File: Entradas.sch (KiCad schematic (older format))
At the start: 20 parts, among them J3 TB_1X3, U1 PS2805-1, U2 PS2805-1, U3 CNY70

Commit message: Se agrego documentacion del proyecto, se agregaron vistas 3d faltantes y se repararon las extensiones de las que no funcionaban
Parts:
- D5, D6: Digikey# (none) -> 160-1446-1-ND
- ENC1: Digikey# (none) -> 987-1188-ND
- J3: Digikey# (none) -> ED2610-ND
- R10, R16, R5, R8, R9: footprint Resistors_SMD:R_1206_HandSoldering -> Resistors_SMD:R_0805_HandSoldering; Digikey# (none) -> RMCF0805JT4K70TR-ND
- R11, R13: footprint Resistors_SMD:R_1206_HandSoldering -> Resistors_SMD:R_0805_HandSoldering; Digikey# (none) -> RMCF0805JT2K20TR-ND
- R12, R14: footprint Resistors_SMD:R_1206_HandSoldering -> Resistors_SMD:R_0805_HandSoldering; Digikey# (none) -> RMCF0805JT100KTR-ND
- R15: footprint Resistors_SMD:R_1206_HandSoldering -> Resistors_SMD:R_0805_HandSoldering; Digikey# (none) -> RMCF0805JT220RTR-ND
- R17: Digikey# (none) -> PTD901-2015K-B502-ND
- R6, R7: footprint Resistors_SMD:R_1206_HandSoldering -> Resistors_SMD:R_0805_HandSoldering; Digikey# (none) -> RMCF0805JT3K30TR-ND
- U1, U2: Digikey# (none) -> PS2805-1ATR-ND
- U3: Digikey# (none) -> 751-1025-ND
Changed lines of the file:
@@
 F 2 "Potentiometers:Potentiometer_Alps-RK16-single_largePads" H 8100 4650 50  0001 C CNN
 F 3 "" H 8100 4650 50  0000 C CNN
+F 4 "PTD901-2015K-B502-ND" H 8100 4650 60  0001 C CNN "Digikey#"
 	1    8100 4650
 	-1   0    0    1
@@
 F 0 "R9" V 2880 4550 50  0000 C CNN
 F 1 "4K7" V 2800 4550 50  0000 C CNN
-F 2 "Resistors_SMD:R_1206_HandSoldering" V 2730 4550 50  0001 C CNN
+F 2 "Resistors_SMD:R_0805_HandSoldering" V 2730 4550 50  0001 C CNN
 F 3 "" H 2800 4550 50  0000 C CNN
+F 4 "RMCF0805JT4K70TR-ND" H 2800 4550 60  0001 C CNN "Digikey#"
 	1    2800 4550
 	-1   0    0    -1
@@
 F 0 "R5" V 2580 4550 50  0000 C CNN
 F 1 "4K7" V 2500 4550 50  0000 C CNN
-F 2 "Resistors_SMD:R_1206_HandSoldering" V 2430 4550 50  0001 C CNN
+F 2 "Resistors_SMD:R_0805_HandSoldering" V 2430 4550 50  0001 C CNN
 F 3 "" H 2500 4550 50  0000 C CNN
+F 4 "RMCF0805JT4K70TR-ND" H 2500 4550 60  0001 C CNN "Digikey#"
 	1    2500 4550
 	-1   0    0    -1
@@
 F 0 "R8" V 2930 2250 50  0000 C CNN
 F 1 "4K7" V 2850 2250 50  0000 C CNN
-F 2 "Resistors_SMD:R_1206_HandSoldering" V 2780 2250 50  0001 C CNN
+F 2 "Resistors_SMD:R_0805_HandSoldering" V 2780 2250 50  0001 C CNN
 F 3 "" H 2850 2250 50  0000 C CNN
+F 4 "RMCF0805JT4K70TR-ND" H 2850 2250 60  0001 C CNN "Digikey#"
 	1    2850 2250
 	1    0    0    -1
@@
 F 0 "R6" V 2680 2050 50  0000 C CNN
 F 1 "3K3" V 2600 2050 50  0000 C CNN
-F 2 "Resistors_SMD:R_1206_HandSoldering" V 2530 2050 50  0001 C CNN
+F 2 "Resistors_SMD:R_0805_HandSoldering" V 2530 2050 50  0001 C CNN
 F 3 "" H 2600 2050 50  0000 C CNN
+F 4 "RMCF0805JT3K30TR-ND" H 2600 2050 60  0001 C CNN "Digikey#"
 	1    2600 2050
 	0    1    1    0
@@
 F 0 "R11" V 4780 1900 50  0000 C CNN
 F 1 "2K2" V 4700 1900 50  0000 C CNN
-F 2 "Resistors_SMD:R_1206_HandSoldering" V 4630 1900 50  0001 C CNN
+F 2 "Resistors_SMD:R_0805_HandSoldering" V 4630 1900 50  0001 C CNN
 F 3 "" H 4700 1900 50  0000 C CNN
+F 4 "RMCF0805JT2K20TR-ND" H 4700 1900 60  0001 C CNN "Digikey#"
 	1    4700 1900
 	0    1    1    0
@@
 F 0 "R12" V 4780 2150 50  0000 C CNN
 F 1 "100K" V 4700 2150 50  0000 C CNN
-F 2 "Resistors_SMD:R_1206_HandSoldering" V 4630 2150 50  0001 C CNN
+F 2 "Resistors_SMD:R_0805_HandSoldering" V 4630 2150 50  0001 C CNN
 F 3 "" H 4700 2150 50  0000 C CNN
+F 4 "RMCF0805JT100KTR-ND" H 4700 2150 60  0001 C CNN "Digikey#"
 	1    4700 2150
 	0    1    1    0
@@
 F 2 "LEDs:LED_0603" H 4200 1900 50  0001 C CNN
 F 3 "" H 4200 1900 50  0000 C CNN
+F 4 "160-1446-1-ND" H 4200 1900 60  0001 C CNN "Digikey#"
 	1    4200 1900
 	1    0    0    -1
@@
 F 2 "Opto-Devices:Optocoupler_SMD_HandSoldering_KPC357_LTV35x_PC357_SingleChannel" H 3236 2076 29  0001 C CNN
 F 3 "" H 3400 2250 60  0000 C CNN
+F 4 "PS2805-1ATR-ND" H 3400 2250 60  0001 C CNN "Digikey#"
 	1    3400 2250
 	1    0    0    -1
@@
 F 2 "footprint:CNY70" H 7400 1950 50  0001 L CIN
 F 3 "" H 7600 2150 50  0000 L CNN
+F 4 "751-1025-ND" H 7600 2150 60  0001 C CNN "Digikey#"
 	1    7600 2150
 	1    0    0    -1
@@
 F 0 "R15" V 7330 2550 50  0000 C CNN
 F 1 "220" V 7250 2550 50  0000 C CNN
-F 2 "Resistors_SMD:R_1206_HandSoldering" V 7180 2550 50  0001 C CNN
+F 2 "Resistors_SMD:R_0805_HandSoldering" V 7180 2550 50  0001 C CNN
 F 3 "" H 7250 2550 50  0000 C CNN
+F 4 "RMCF0805JT220RTR-ND" H 7250 2550 60  0001 C CNN "Digikey#"
 	1    7250 2550
 	1    0    0    -1
@@
 F 0 "R16" V 8030 2550 50  0000 C CNN
 F 1 "4K7" V 7950 2550 50  0000 C CNN
-F 2 "Resistors_SMD:R_1206_HandSoldering" V 7880 2550 50  0001 C CNN
+F 2 "Resistors_SMD:R_0805_HandSoldering" V 7880 2550 50  0001 C CNN
 F 3 "" H 7950 2550 50  0000 C CNN
+F 4 "RMCF0805JT4K70TR-ND" H 7950 2550 60  0001 C CNN "Digikey#"
 	1    7950 2550
 	1    0    0    -1
@@
 F 2 "footprint:Encoder_rotativo" H 3700 5050 50  0001 C CNN
 F 3 "" H 3700 5050 50  0000 C CNN
+F 4 "987-1188-ND" H 3700 5050 60  0001 C CNN "Digikey#"
 	1    3700 5050
 	-1   0    0    -1
@@
 F 0 "R10" V 2930 3000 50  0000 C CNN
 F 1 "4K7" V 2850 3000 50  0000 C CNN
-F 2 "Resistors_SMD:R_1206_HandSoldering" V 2780 3000 50  0001 C CNN
+F 2 "Resistors_SMD:R_0805_HandSoldering" V 2780 3000 50  0001 C CNN
 F 3 "" H 2850 3000 50  0000 C CNN
+F 4 "RMCF0805JT4K70TR-ND" H 2850 3000 60  0001 C CNN "Digikey#"
 	1    2850 3000
 	1    0    0    -1
@@
 F 0 "R7" V 2680 2800 50  0000 C CNN
 F 1 "3K3" V 2600 2800 50  0000 C CNN
-F 2 "Resistors_SMD:R_1206_HandSoldering" V 2530 2800 50  0001 C CNN
+F 2 "Resistors_SMD:R_0805_HandSoldering" V 2530 2800 50  0001 C CNN
 F 3 "" H 2600 2800 50  0000 C CNN
+F 4 "RMCF0805JT3K30TR-ND" H 2600 2800 60  0001 C CNN "Digikey#"
 	1    2600 2800
 	0    1    1    0
@@
 F 0 "R13" V 4780 2650 50  0000 C CNN
 F 1 "2K2" V 4700 2650 50  0000 C CNN
-F 2 "Resistors_SMD:R_1206_HandSoldering" V 4630 2650 50  0001 C CNN
+F 2 "Resistors_SMD:R_0805_HandSoldering" V 4630 2650 50  0001 C CNN
 F 3 "" H 4700 2650 50  0000 C CNN
+F 4 "RMCF0805JT2K20TR-ND" H 4700 2650 60  0001 C CNN "Digikey#"
 	1    4700 2650
 	0    1    1    0
@@
 F 0 "R14" V 4780 2900 50  0000 C CNN
 F 1 "100K" V 4700 2900 50  0000 C CNN
-F 2 "Resistors_SMD:R_1206_HandSoldering" V 4630 2900 50  0001 C CNN
+F 2 "Resistors_SMD:R_0805_HandSoldering" V 4630 2900 50  0001 C CNN
 F 3 "" H 4700 2900 50  0000 C CNN
+F 4 "RMCF0805JT100KTR-ND" H 4700 2900 60  0001 C CNN "Digikey#"
 	1    4700 2900
 	0    1    1    0
@@
 F 2 "LEDs:LED_0603" H 4200 2650 50  0001 C CNN
 F 3 "" H 4200 2650 50  0000 C CNN
+F 4 "160-1446-1-ND" H 4200 2650 60  0001 C CNN "Digikey#"
 	1    4200 2650
 	1    0    0    -1
@@
 F 2 "Opto-Devices:Optocoupler_SMD_HandSoldering_KPC357_LTV35x_PC357_SingleChannel" H 3236 2826 29  0001 C CNN
 F 3 "" H 3400 3000 60  0000 C CNN
+F 4 "PS2805-1ATR-ND" H 3400 3000 60  0001 C CNN "Digikey#"
 	1    3400 3000
 	1    0    0    -1
@@
 F 2 "Terminal_Blocks:TerminalBlock_Pheonix_MPT-2.54mm_3pol" H 1350 2500 60  0001 C CNN
 F 3 "" H 1350 2500 60  0000 C CNN
+F 4 "ED2610-ND" H 1400 2450 60  0001 C CNN "Digikey#"
 	1    1400 2450
 	1    0    0    -1

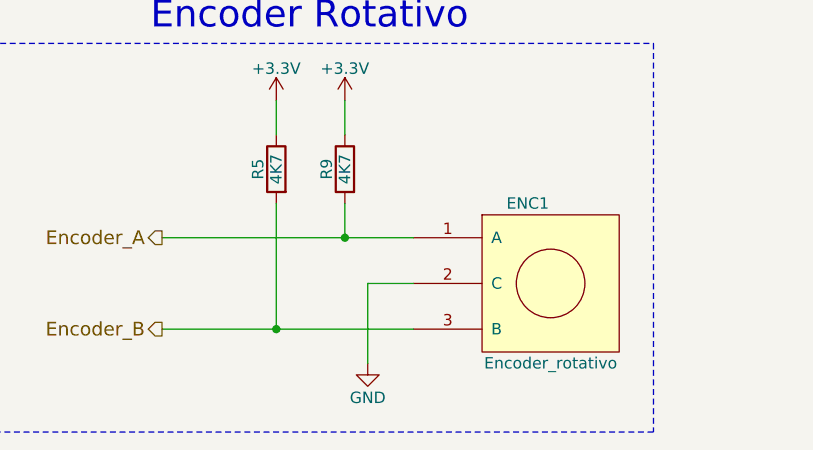
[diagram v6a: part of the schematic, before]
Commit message: Correcion de pistas a octoacopladores, rutas de modelos 3d, id encoder y otras correcciones menores
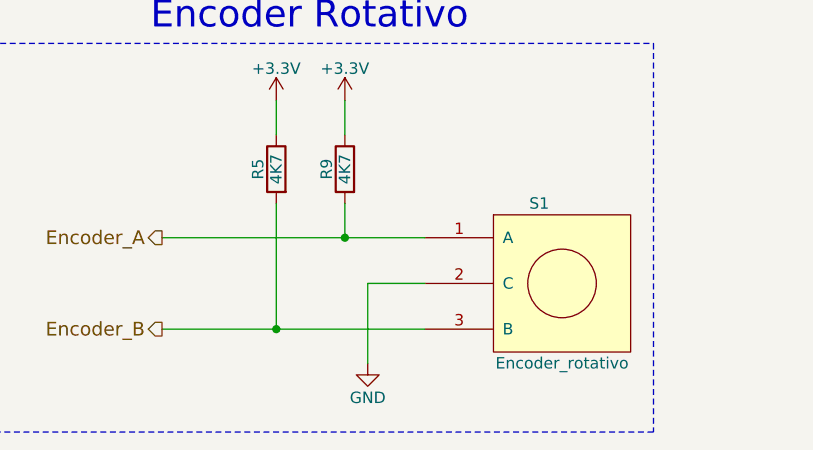
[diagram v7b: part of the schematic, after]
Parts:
- removed ENC1: Encoder_rotativo, footprint:Encoder_rotativo, symbol Encoder_rotativo
- added S1: Encoder_rotativo, footprint:Encoder_rotativo, symbol Encoder_rotativo
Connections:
- net Encoder_A: now also S1.1 (A)
- net Encoder_B: now also S1.3 (B)
- net GND: now also S1.2 (C)
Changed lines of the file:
@@
 Sheet 2 4
 Title "Entradas- EduPoncho"
-Date "2016-11-17"
+Date "2016-12-19"
 Rev ""
 Comp "Proyecto CIAA - COMPUTADORA INDUSTRIAL ABIERTA ARGENTINA"
@@
 	1    0    0    -1
 $EndComp
-$Comp
-L Encoder_rotativo ENC1
-U 1 1 584E0465
-P 3700 5050
-F 0 "ENC1" H 3800 5400 50  0000 C CNN
-F 1 "Encoder_rotativo" H 3700 4701 50  0000 C CNN
-F 2 "footprint:Encoder_rotativo" H 3700 5050 50  0001 C CNN
-F 3 "" H 3700 5050 50  0000 C CNN
-F 4 "987-1188-ND" H 3700 5050 60  0001 C CNN "Digikey#"
-	1    3700 5050
-	-1   0    0    -1
-$EndComp
-Wire Wire Line
-	3100 5050 2900 5050
-Wire Wire Line
-	2000 5250 3100 5250
-Wire Wire Line
-	2000 4850 3100 4850
+Wire Wire Line
+	2900 5050 3150 5050
+Wire Wire Line
+	2000 5250 3150 5250
+Wire Wire Line
+	2000 4850 3150 4850
 Text HLabel 5450 3050 2    60   Output ~ 0
 OPTO_IN1
@@
 Wire Wire Line
 	3850 2350 3850 2400
+$Comp
+L Encoder_rotativo S1
+U 1 1 58585C66
+P 3750 5050
+F 0 "S1" H 3850 5400 50  0000 C CNN
+F 1 "Encoder_rotativo" H 3750 4701 50  0000 C CNN
+F 2 "footprint:Encoder_rotativo" H 3750 5050 50  0001 C CNN
+F 3 "" H 3750 5050 50  0000 C CNN
+	1    3750 5050
+	-1   0    0    -1
+$EndComp
 $EndSCHEMATC
